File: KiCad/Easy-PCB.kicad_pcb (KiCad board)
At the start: 2 copper layers, 203.2 x 83.8 mm, 99 parts, among them J1 703W-00/53, J3 HLW20R-2C7LF, K1 G5LE-1A-E_DC12, P1 1x02, P12 M20-9980346, P2 1x06, P24 M20-9980346, P3 1x04, P4 1x03 Terminal Block, P5 1x02, P6 via, P7 via, Q1 2N3904, Q10 MJE350, Q11 2N3904, Q12 2N3904, Q13 MJE340, Q14 MJE350, Q15 2N3904, Q16 MJE340, Q17 MJE350, Q18 2N3904, Q19 2N3904, Q2 MJE340, Q3 2N3904, Q4 2N3904, Q5 MJE340, Q6 MJE350, Q7 2N3904, Q8 2N3904, Q9 MJE340, SW1 R1966ABLKBLKFR, T1 VPP24-830, U1 PIC16F883, U2 MCP41050, U3 MCP617, U4 MCP9700A, U5 LM7805

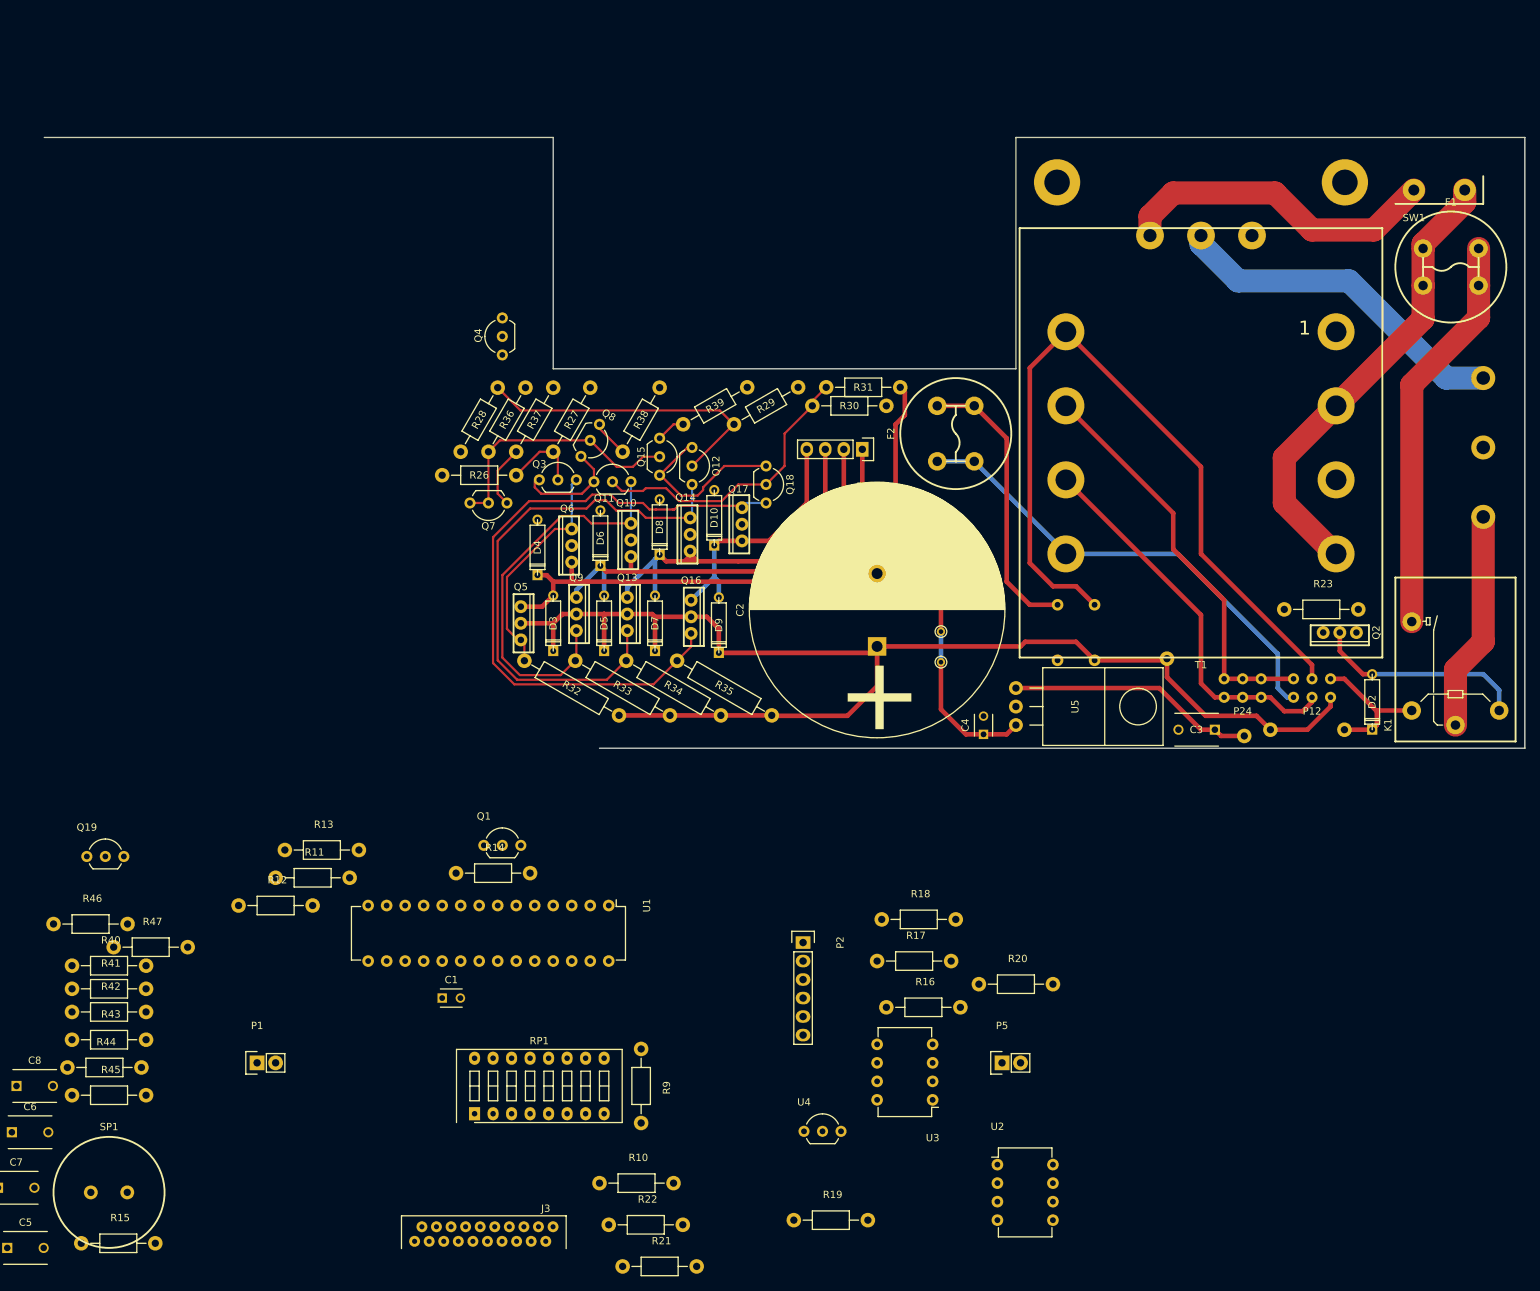
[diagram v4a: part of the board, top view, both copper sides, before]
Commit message: reconfigured motor driver routing
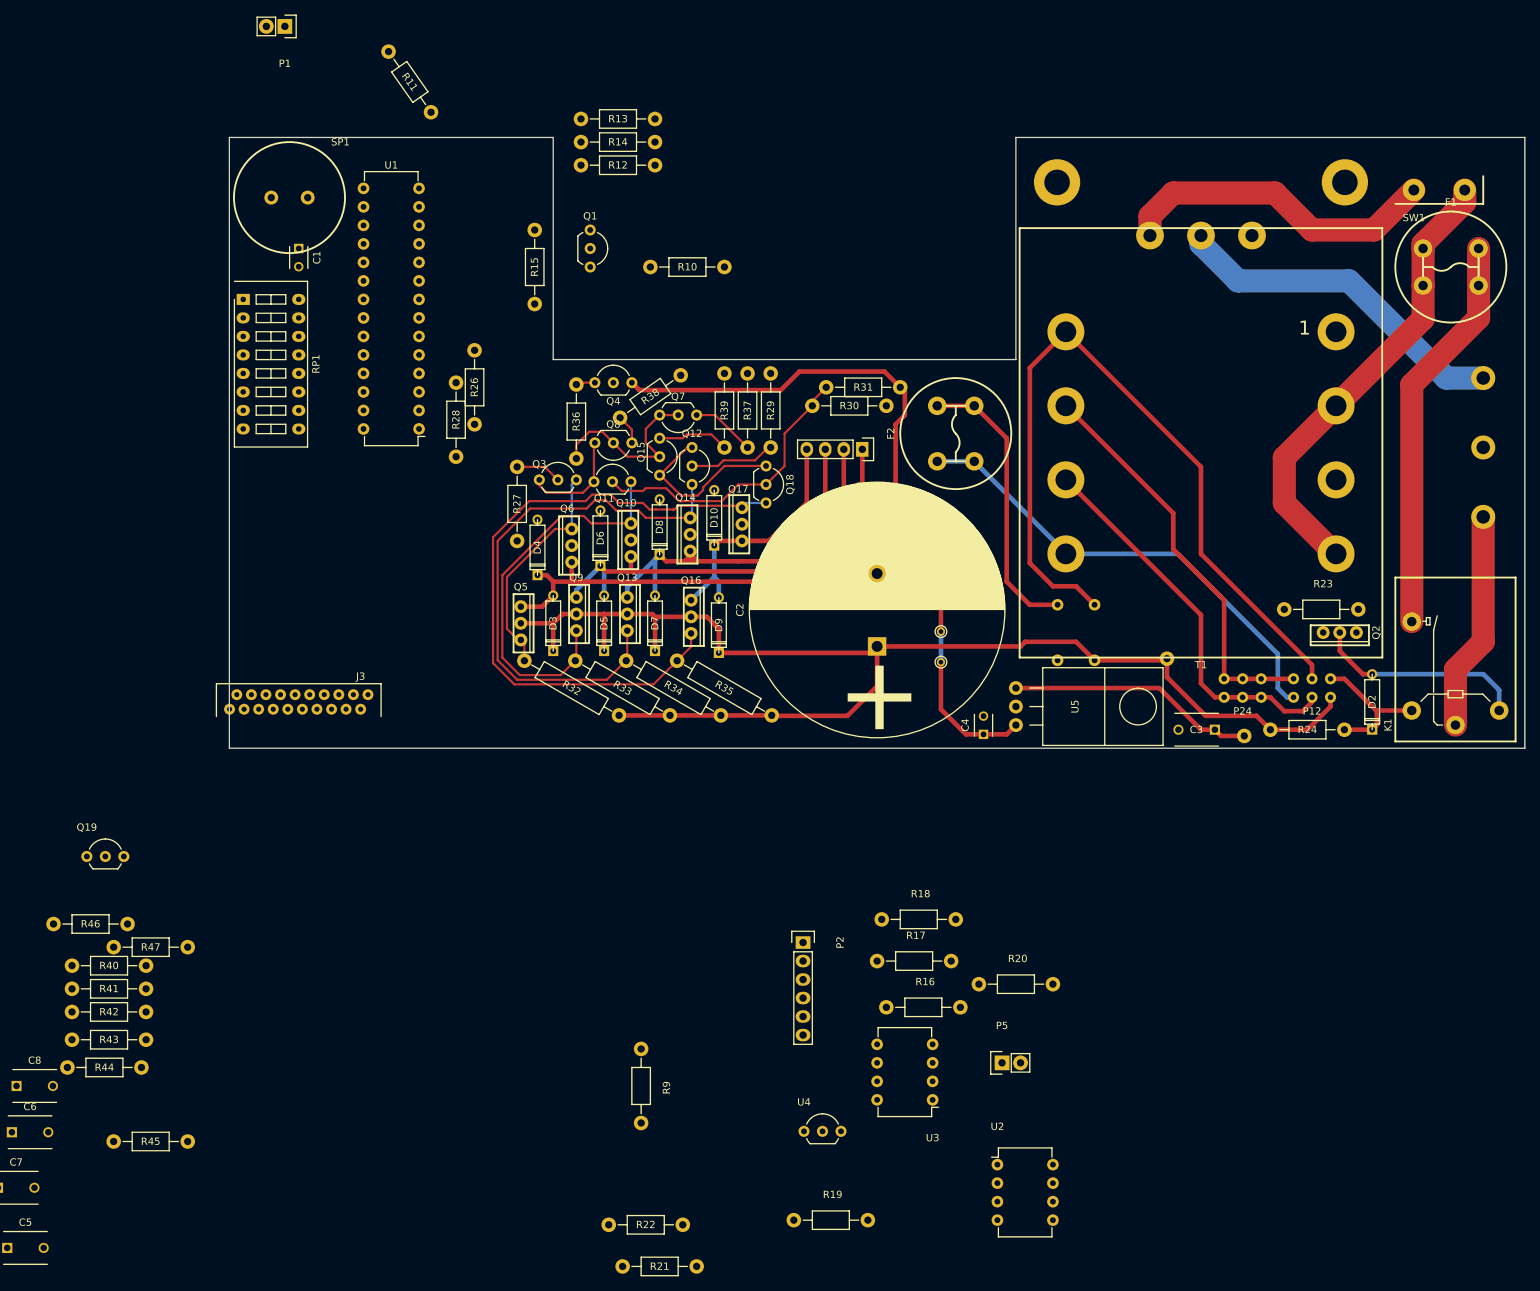
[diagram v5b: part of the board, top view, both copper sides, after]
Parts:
- R24: moved to F.Cu
- moved R15 145.7 mm to (92.7, 55.9), turned to 90 degrees
- moved P1 142.3 mm to (58.4, 22.9), turned to 180 degrees
- moved SP1 138.8 mm to (59.1, 46.4)
- moved R10 125.9 mm to (113.7, 55.9), turned to 180 degrees
- moved RP1 116.2 mm to (52.7, 60.3), turned to 270 degrees
- moved R12 111.9 mm to (104.1, 41.9), turned to 180 degrees
- moved R11 110.0 mm to (75.6, 30.5), turned to 125 degrees
- moved R13 108.2 mm to (104.1, 35.6), turned to 180 degrees
- moved C1 104.7 mm to (60.3, 53.3), turned to 270 degrees
- moved R14 101.8 mm to (104.1, 38.7), turned to 180 degrees
- moved Q1 85.7 mm to (100.3, 50.8), turned to 270 degrees
- moved J3 77.3 mm to (60.3, 115.6)
- moved U1 70.4 mm to (76.8, 78.1), turned to 180 degrees
- moved R37 29.2 mm to (121.9, 75.6), turned to 90 degrees
- moved Q7 28.7 mm to (114.9, 76.2)
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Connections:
- U1 pad 12: /Motor Driver/wind2 -> /Motor Driver/wind1
- U1 pad 13: /Motor Driver/wind1 -> /Motor Driver/wind2
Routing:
- net VDD: track 59.8 -> 99.0 mm
- net Net-(Q12-Pad2): track 42.6 -> 11.8 mm
- net Net-(Q15-Pad2): track 35.8 -> 25.3 mm
- net Net-(Q15-Pad1): track 4.01 -> 9.84 mm
- net Net-(Q3-Pad2): track 10.5 -> 6.32 mm
- net Net-(Q4-Pad1): track 0.00 -> 2.65 mm
- net Net-(Q8-Pad1): track 5.08 -> 4.11 mm
- net Net-(Q7-Pad1): track 8.61 -> 9.46 mm
- net Net-(Q11-Pad1): track 14.2 -> 14.9 mm
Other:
- board size 203.2 x 83.8 mm -> 177.8 x 83.8 mm

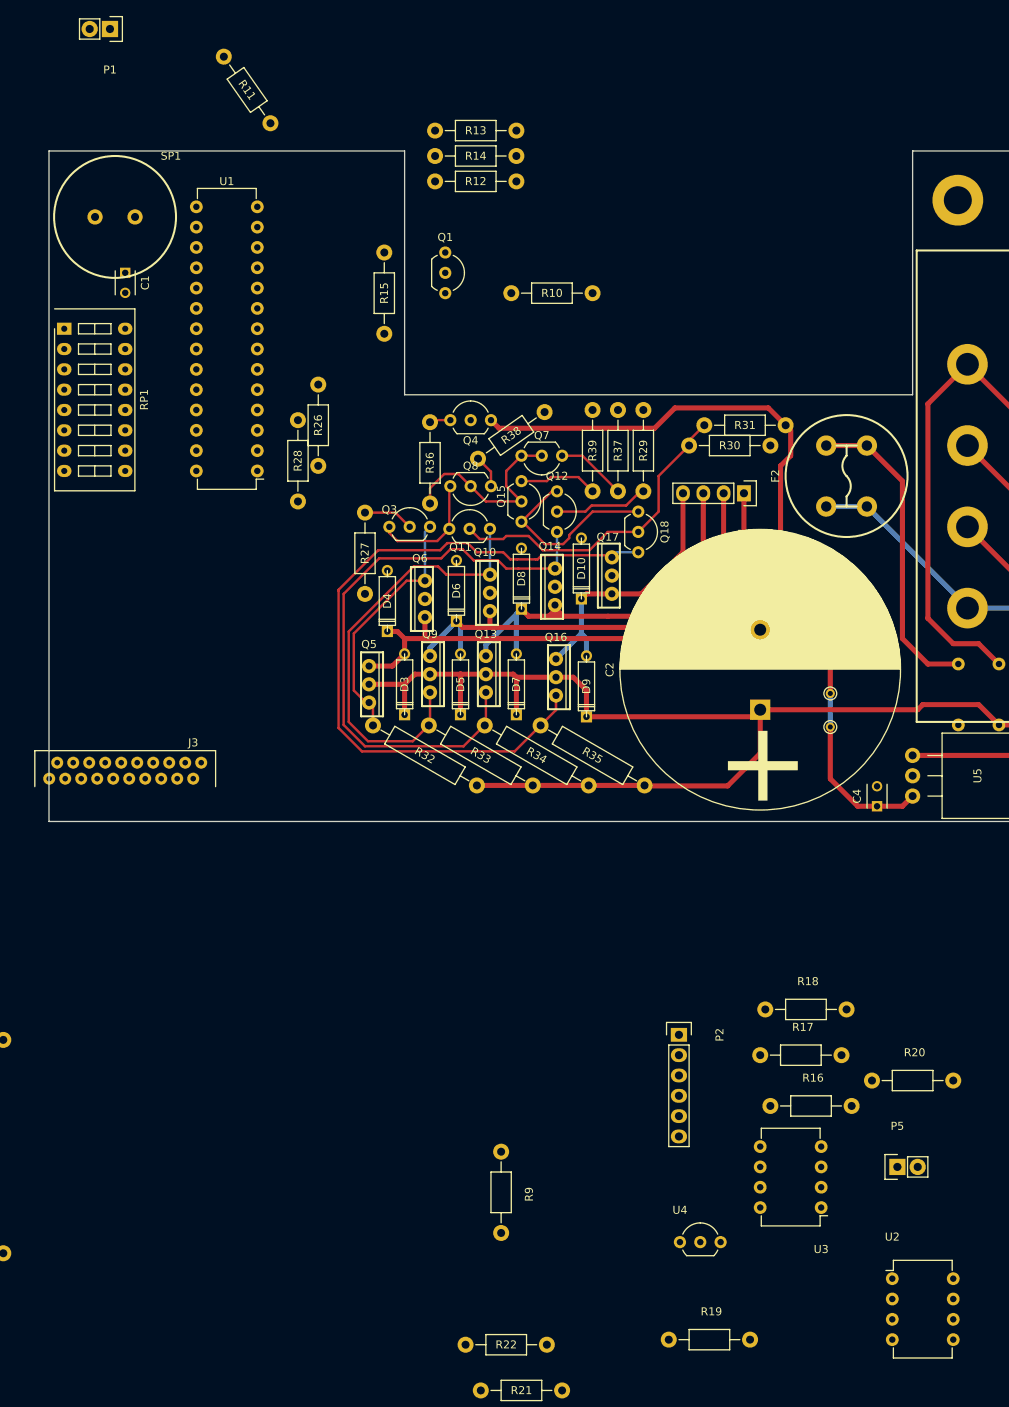
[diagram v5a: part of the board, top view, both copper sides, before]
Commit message: most of temperature feedback in place
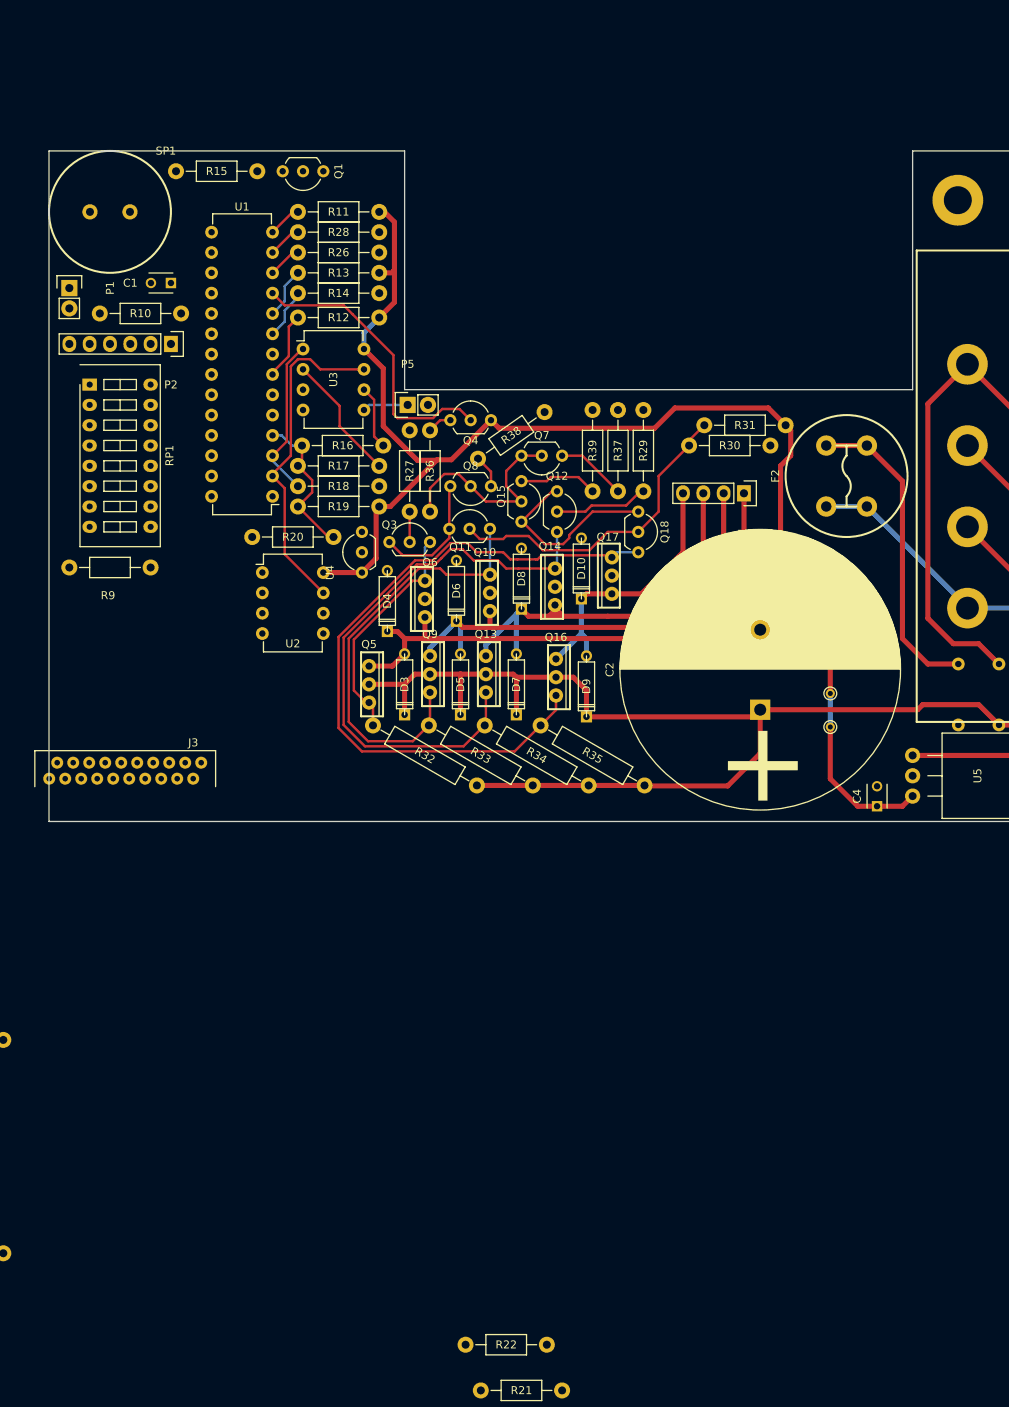
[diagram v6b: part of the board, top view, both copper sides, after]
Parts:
- moved U3 125.3 mm to (82.5, 62.9), turned to 0 degrees
- moved U2 118.3 mm to (77.5, 90.8)
- moved R19 114.0 mm to (87.0, 82.5), turned to 180 degrees
- moved P5 113.2 mm to (95.6, 69.8)
- moved P2 107.2 mm to (66.0, 62.2), turned to 180 degrees
- moved R20 103.0 mm to (81.3, 86.4), turned to 180 degrees
- moved R16 101.2 mm to (87.5, 74.9)
- moved R17 93.6 mm to (87.0, 77.5)
- moved U4 92.7 mm to (89.9, 90.8), turned to 90 degrees
- moved R9 92.1 mm to (58.4, 90.2), turned to 180 degrees
- moved R18 87.7 mm to (87.0, 80.0), turned to 180 degrees
- moved R10 51.5 mm to (62.2, 58.4), turned to 0 degrees
- moved P1 32.8 mm to (53.3, 55.2), turned to 270 degrees
- moved R28 29.0 mm to (87.0, 48.3), turned to 180 degrees
- moved R15 25.9 mm to (71.8, 40.6), turned to 0 degrees
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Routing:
- net VDD: track 99.0 -> 172.8 mm
- net /Temperature Feedback/Tk: track 0.00 -> 41.9 mm
- net /Motor Driver/Motor_On: track 0.00 -> 36.6 mm
- net /Temperature Feedback/Tref: track 0.00 -> 21.6 mm
- net /Temperature Feedback/Vref-: track 0.00 -> 19.5 mm
- net Net-(R17-Pad2): track 0.00 -> 16.0 mm
- net CS1: track 0.00 -> 8.43 mm
- net Net-(R16-Pad2): track 0.00 -> 7.98 mm
- net CS2: track 0.00 -> 6.40 mm
- net Net-(R14-Pad2): track 0.00 -> 6.40 mm
- net /Temperature Feedback/K+: track 0.00 -> 5.72 mm
- net /Motor Driver/wind1: track 0.00 -> 4.23 mm
- net SCK: track 0.00 -> 4.23 mm
- net /Motor Driver/wind2: track 0.00 -> 4.23 mm
- net Net-(Q16-Pad3): track 90.9 -> 87.5 mm
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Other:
- outline, holes or cut-outs redrawn
